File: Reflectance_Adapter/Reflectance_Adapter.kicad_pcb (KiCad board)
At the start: 2 copper layers, 4 parts, among them J1 Reflector I2C, J2 Conn_QTRX_Top_Row, J3 Conn_QTRX_Bot_Row, U1 TCA9555PWR

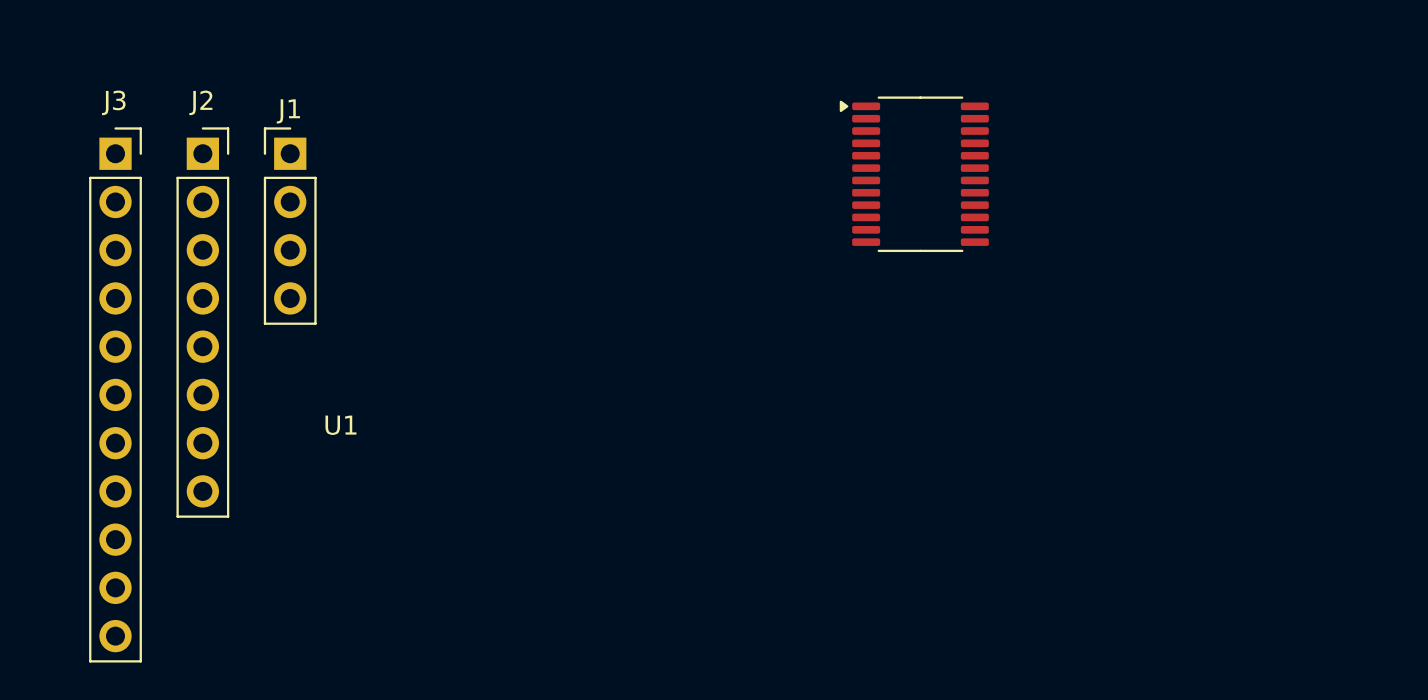
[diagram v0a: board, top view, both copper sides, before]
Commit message: Completed layout
User layer 1 contains dimensions of Pololu reflectance sensor array board. User layer 8 contains dimensions of slots of Pololu Chassis (copied over from the MSPM0 kicad project)
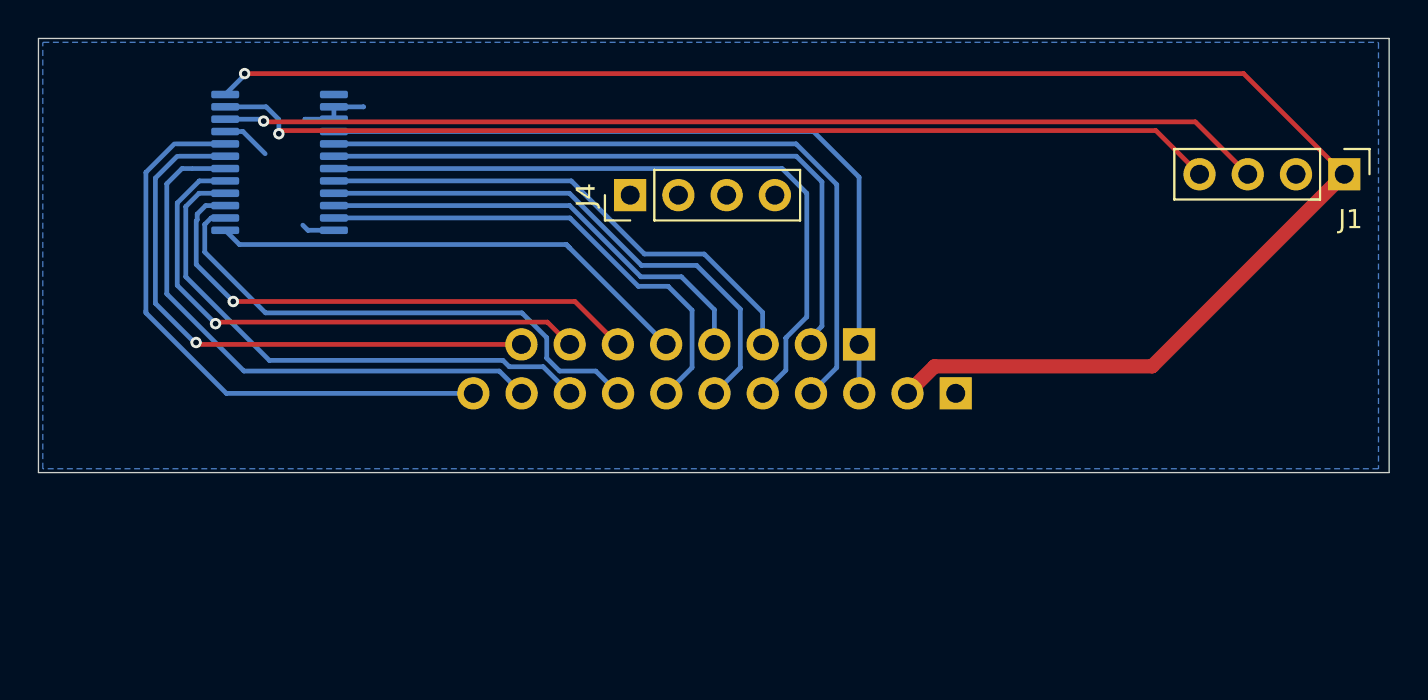
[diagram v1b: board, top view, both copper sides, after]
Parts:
- added J4: Support, Connector_PinHeader_2.54mm:PinHeader_1x04_P2.54mm_Vertical, F.Cu at (129.1, 97.1)
- J2, J3, U1: moved to B.Cu
- moved J1 55.5 mm to (166.7, 96.0), turned to -90 degrees
- moved J3 46.0 mm to (146.2, 107.5), turned to 90 degrees
- moved J2 36.0 mm to (141.2, 105.0), turned to 90 degrees
- moved U1 33.8 mm to (110.6, 95.4), turned to 180 degrees
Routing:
- net +3V3: track 0.00 -> 89.4 mm, vias 0 -> 1
- net /SCL: track 0.00 -> 55.0 mm, vias 0 -> 1
- net /SDA: track 0.00 -> 53.4 mm, vias 0 -> 1
- net /LED_ctrl: track 0.00 -> 40.0 mm
- net /1: track 0.00 -> 38.9 mm
- net /3: track 0.00 -> 36.9 mm
- net /2: track 0.00 -> 35.1 mm
- net /15: track 0.00 -> 31.1 mm
- net /14: track 0.00 -> 30.8 mm, vias 0 -> 1
- net /13: track 0.00 -> 30.0 mm
- net /12: track 0.00 -> 29.4 mm, vias 0 -> 1
- net /5: track 0.00 -> 28.9 mm
- net /11: track 0.00 -> 28.8 mm
- net /10: track 0.00 -> 28.3 mm, vias 0 -> 1
- net /9: track 0.00 -> 28.2 mm
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- added copper zone on B.Cu, net GND
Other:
- board outline added: 71.1 x 22.9 mm
- board text added: "QTRX-HD-15RC Board Outline"

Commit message: Added text to silkscreen
Also generated Gerbers
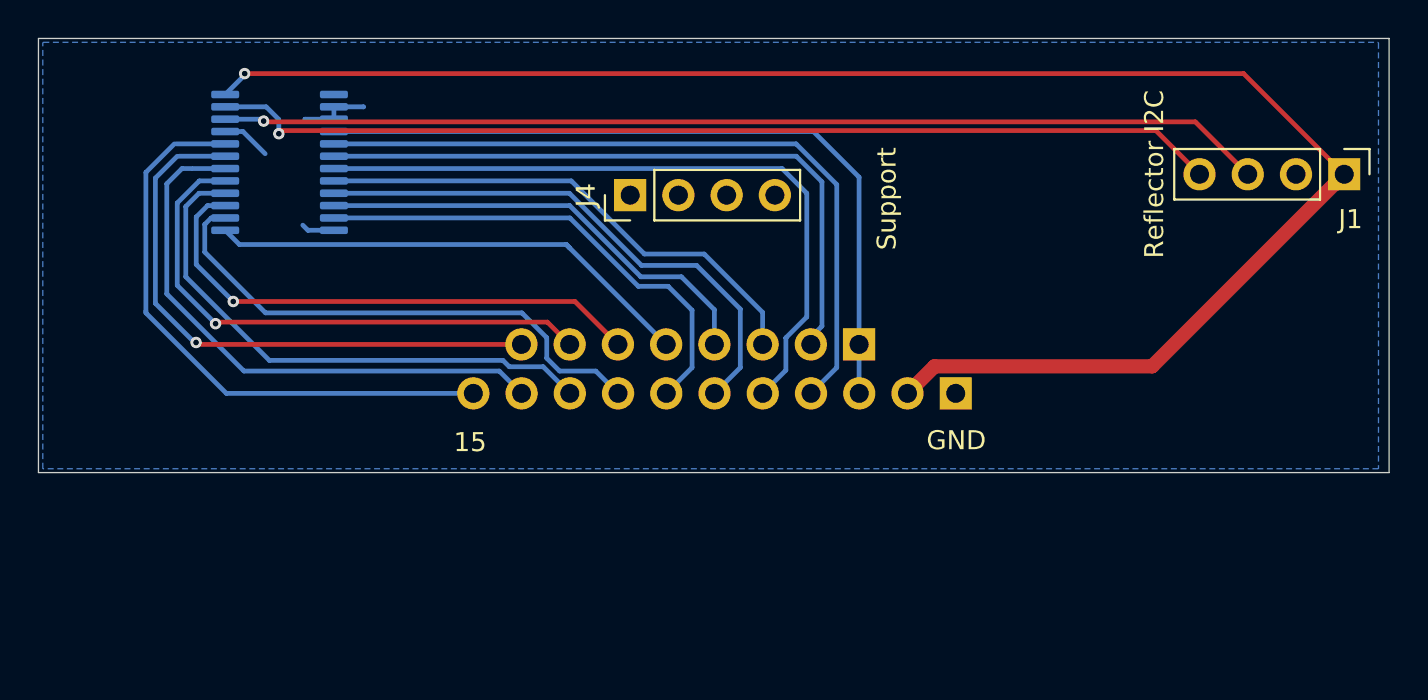
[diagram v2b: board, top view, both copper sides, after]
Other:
- board text added: "15"
- board text added: "GND"
- board text added: "Reflector I2C"
- board text added: "Support"
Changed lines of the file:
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@@
 			(plot_on_all_layers_selection 0x0000000_00000000)
 			(disableapertmacros no)
-			(usegerberextensions no)
+			(usegerberextensions yes)
 			(usegerberattributes yes)
 			(usegerberadvancedattributes yes)
@@
 			(outputformat 1)
 			(mirror no)
-			(drillshape 1)
+			(drillshape 0)
 			(scaleselection 1)
-			(outputdirectory "")
+			(outputdirectory "Gerber/")
 		)
 	)
@@
 		)
 		(fp_text user "${REFERENCE}"
-			(at 0 3.81 360)
+			(at 0 3.81 0)
 			(layer "F.Fab")
 			(effects
@@
 		)
 		(property "Value" "Support"
-			(at 0 9.95 90)
+			(at 0 13.5 90)
 			(layer "F.Fab")
 			(effects
@@
 		)
 		(fp_text user "${REFERENCE}"
-			(at 0 3.81 360)
+			(at 0 3.81 0)
 			(layer "F.Fab")
 			(effects
@@
 		(tags "TSSOP SO")
 		(property "Reference" "U1"
-			(at -6.8 -0.2 360)
+			(at -6.8 -0.2 0)
 			(layer "B.SilkS")
 			(effects
@@
 		)
 		(property "Value" "TCA9555PWR"
-			(at 0 -4.85 360)
+			(at 0 -4.85 0)
 			(layer "B.Fab")
 			(effects
@@
 		)
 		(property "Footprint" "Package_SO:TSSOP-24_4.4x7.8mm_P0.65mm"
-			(at 0 0 360)
+			(at 0 0 0)
 			(layer "B.Fab")
 			(hide yes)
@@
 		)
 		(property "Datasheet" "http://www.ti.com/lit/ds/symlink/tca9555.pdf"
-			(at 0 0 360)
+			(at 0 0 0)
 			(layer "B.Fab")
 			(hide yes)
@@
 		)
 		(property "Description" "16-bit I/O expander, I2C and SMBus interface, interrupts, w/ pull-ups, TSSOP-24 package"
-			(at 0 0 360)
+			(at 0 0 0)
 			(layer "B.Fab")
 			(hide yes)
@@
 		)
 		(fp_text user "${REFERENCE}"
-			(at -6.8 -2.3 360)
+			(at -6.8 -2.3 0)
 			(layer "B.Fab")
 			(effects
@@
 		(layer "User.8")
 	)
+	(gr_text "15"
+		(at 119.8 110.7 0)
+		(layer "F.SilkS")
+		(effects
+			(font
+				(size 1 1)
+				(thickness 0.1524)
+			)
+			(justify left bottom)
+		)
+	)
+	(gr_text "Reflector I2C"
+		(at 156.7 96 90)
+		(layer "F.SilkS")
+		(effects
+			(font
+				(size 1 1)
+				(thickness 0.1524)
+			)
+		)
+	)
+	(gr_text "Support"
+		(at 143.2 100 90)
+		(layer "F.SilkS")
+		(effects
+			(font
+				(size 1 1)
+				(thickness 0.1524)
+			)
+			(justify left bottom)
+		)
+	)
+	(gr_text "GND"
+		(at 144.7 110.6 0)
+		(layer "F.SilkS")
+		(effects
+			(font
+				(size 1 1)
+				(thickness 0.1524)
+			)
+			(justify left bottom)
+		)
+	)
 	(gr_text "QTRX-HD-15RC Board Outline\n"
 		(at 141.2 111 0)
@@
 	)
 	(segment
-		(start 106.3 98.1)
-		(end 106.3 98.4)
-		(width 0.249936)
-		(layer "B.Cu")
-		(net 10)
-	)
-	(segment
-		(start 106.250064 98.449936)
-		(end 106.250064 100.750064)
-		(width 0.249936)
-		(layer "B.Cu")
-		(net 10)
-	)
-	(segment
-		(start 106.3 98.4)
-		(end 106.250064 98.449936)
-		(width 0.249936)
-		(layer "B.Cu")
-		(net 10)
-	)
-	(segment
-		(start 106.75 97.65)
-		(end 106.3 98.1)
+		(start 107.775 97.65)
+		(end 106.85 97.65)
 		(width 0.249936)
 		(layer "B.Cu")
@@
 	)
 	(segment
-		(start 107.775 97.65)
-		(end 106.75 97.65)
-		(width 0.249936)
-		(layer "B.Cu")
+		(start 106.250064 98.249936)
+		(end 106.250064 100.750064)
+		(width 0.249936)
+		(layer "B.Cu")
+		(net 10)
+	)
+	(segment
+		(start 106.85 97.65)
+		(end 106.250064 98.249936)
+		(width 0.249936)
+		(layer "B.Cu")

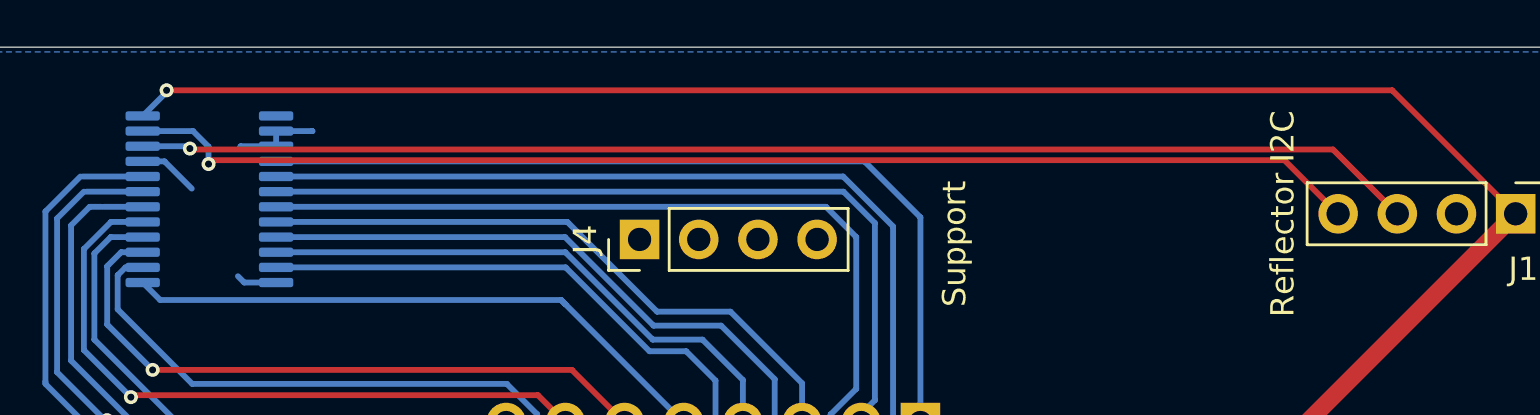
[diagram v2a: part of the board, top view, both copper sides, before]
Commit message: corrected i2c pin positions
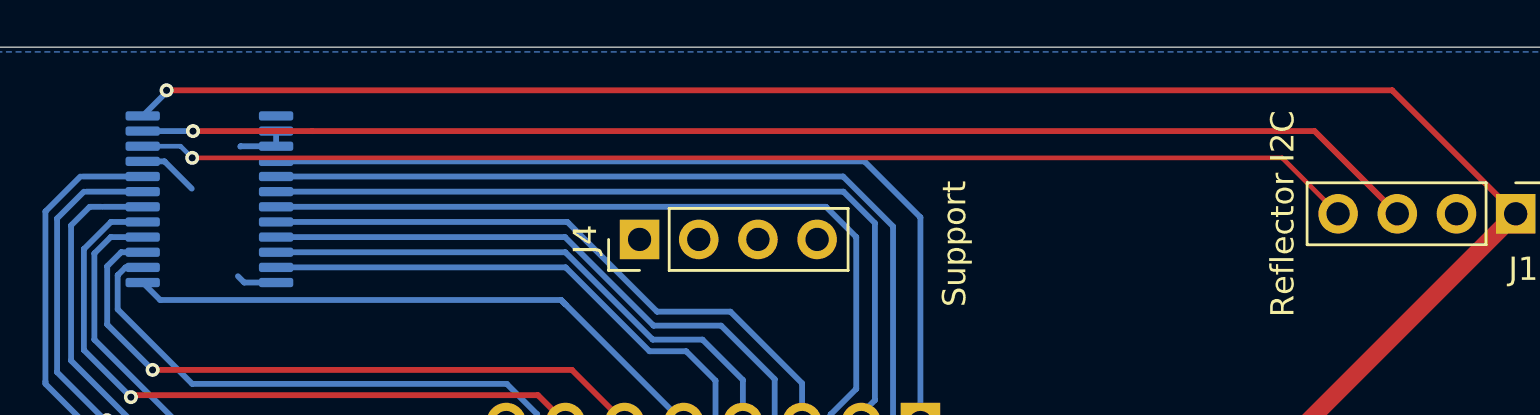
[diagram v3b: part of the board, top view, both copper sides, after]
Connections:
- J1 pad 3: /SCL -> /SDA
- J1 pad 4: /SDA -> /SCL
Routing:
- net /SCL: track 55.0 -> 52.5 mm
- net /SDA: track 53.4 -> 55.3 mm
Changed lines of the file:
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@@
 			(layers "*.Cu" "*.Mask")
 			(remove_unused_layers no)
-			(net 2 "/SCL")
+			(net 4 "/SDA")
 			(pinfunction "Pin_3")
 			(pintype "passive")
@@
 			(layers "*.Cu" "*.Mask")
 			(remove_unused_layers no)
-			(net 4 "/SDA")
+			(net 2 "/SCL")
 			(pinfunction "Pin_4")
 			(pintype "passive")
@@
 		)
 		(height 3.2)
-		(gr_text "681.1024 mils"
+		(gr_text "17.3000 mm"
 			(at 155.25 106.44764 0)
 			(layer "B.Fab")
@@
 		)
 		(height 7.1)
-		(gr_text "31.4961 mils"
+		(gr_text "0.8000 mm"
 			(at 152.05 104.09764 90)
 			(layer "B.Fab")
@@
 		)
 		(height -9.8)
-		(gr_text "100.0000 mils"
+		(gr_text "2.5400 mm"
 			(at 114.85 106.26764 90)
 			(layer "B.Fab")
@@
 		)
 		(height -15.621)
-		(gr_text "200.0000 mils"
+		(gr_text "5.0800 mm"
 			(at 166.5224 87.7246 0)
 			(layer "User.1")
@@
 		)
 		(height 8.0772)
-		(gr_text "200.0000 mils"
+		(gr_text "5.0800 mm"
 			(at 100.4062 82.3144 0)
 			(layer "User.1")
@@
 	)
 	(segment
-		(start 161.62 96)
-		(end 158.86 93.24)
-		(width 0.249936)
+		(start 156.68 93.6)
+		(end 159.08 96)
+		(width 0.2)
 		(layer "F.Cu")
 		(net 2)
 	)
 	(segment
-		(start 109.84 93.24)
-		(end 158.86 93.24)
-		(width 0.249936)
+		(start 109.9 93.6)
+		(end 156.68 93.6)
+		(width 0.2)
 		(layer "F.Cu")
 		(net 2)
 	)
-	(segment
-		(start 109.8 93.2)
-		(end 109.84 93.24)
-		(width 0.249936)
-		(layer "F.Cu")
-		(net 2)
-	)
 	(via
-		(at 109.8 93.2)
+		(at 109.9 93.6)
 		(size 0.6)
 		(drill 0.3)
@@
 	)
 	(segment
-		(start 109.7 93.1)
-		(end 107.775 93.1)
-		(width 0.249936)
+		(start 107.775 93.1)
+		(end 109.4 93.1)
+		(width 0.2)
 		(layer "B.Cu")
 		(net 2)
 	)
 	(segment
-		(start 109.8 93.2)
-		(end 109.7 93.1)
-		(width 0.249936)
+		(start 109.4 93.1)
+		(end 109.9 93.6)
+		(width 0.2)
 		(layer "B.Cu")
 		(net 2)
@@
 	)
 	(segment
-		(start 156.78 93.7)
-		(end 110.6 93.7)
+		(start 109.933839 92.45)
+		(end 158.07 92.45)
 		(width 0.249936)
 		(layer "F.Cu")
@@
 	)
 	(segment
-		(start 159.08 96)
-		(end 156.78 93.7)
+		(start 158.07 92.45)
+		(end 161.62 96)
 		(width 0.249936)
 		(layer "F.Cu")
 		(net 4)
 	)
-	(segment
-		(start 110.6 93.7)
-		(end 110.6 93.864968)
-		(width 0.249936)
-		(layer "F.Cu")
-		(net 4)
-	)
 	(via
-		(at 110.6 93.864968)
+		(at 109.933839 92.45)
 		(size 0.6)
 		(drill 0.3)
@@
 		(net 4)
 	)
-	(segment
-		(start 110.6 93.116161)
-		(end 109.933839 92.45)
-		(width 0.249936)
-		(layer "B.Cu")
-		(net 4)
-	)
-	(segment
-		(start 110.6 93.864968)
-		(end 110.6 93.116161)
-		(width 0.249936)
-		(layer "B.Cu")
-		(net 4)
-	)
